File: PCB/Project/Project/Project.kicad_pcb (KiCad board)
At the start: 2 copper layers, 72.4 x 71.1 mm, 10 parts, among them J1 Conn_01x03_Male, J2 DB9_Female, SW1 SW_Push, U1 ESP32-DEVKIT-V1

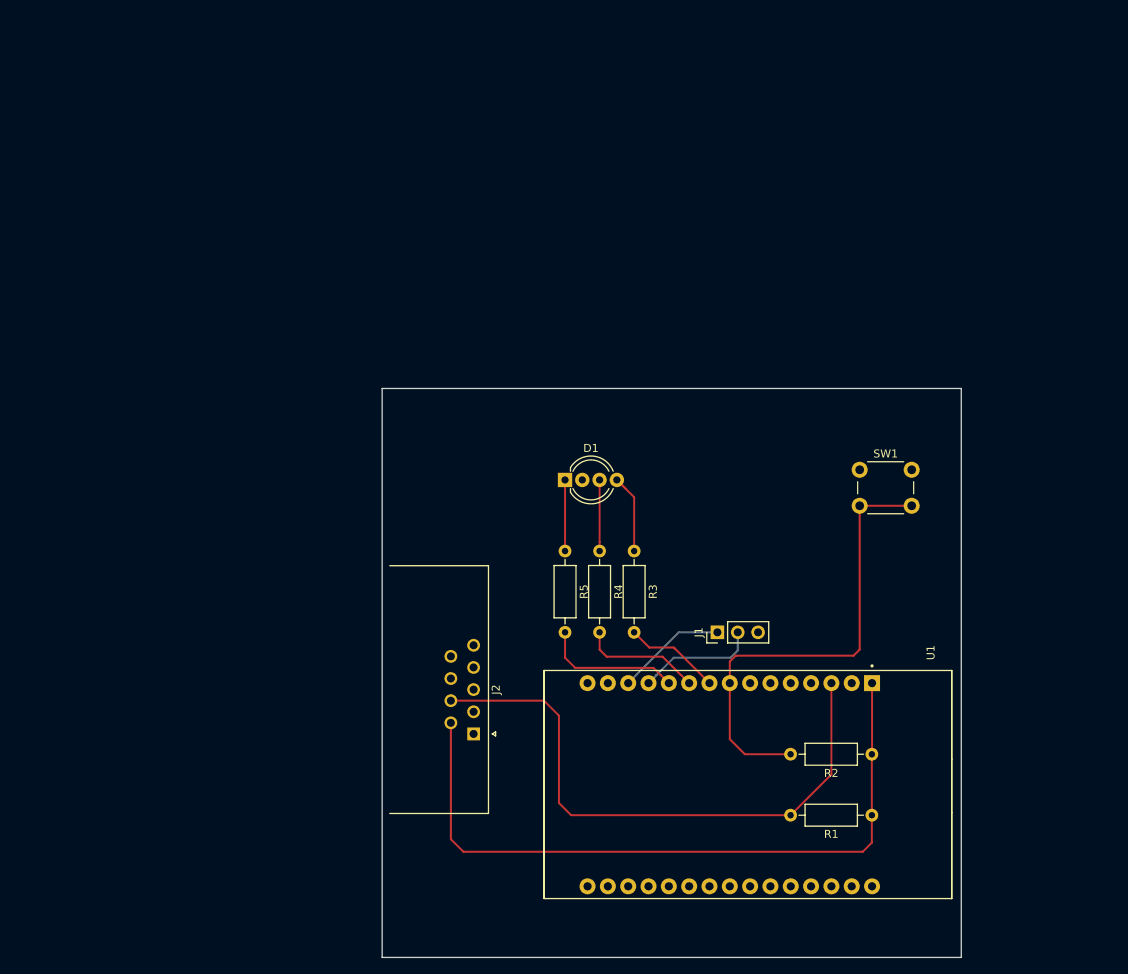
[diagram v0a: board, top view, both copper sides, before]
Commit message: New PCB. Added design rules.
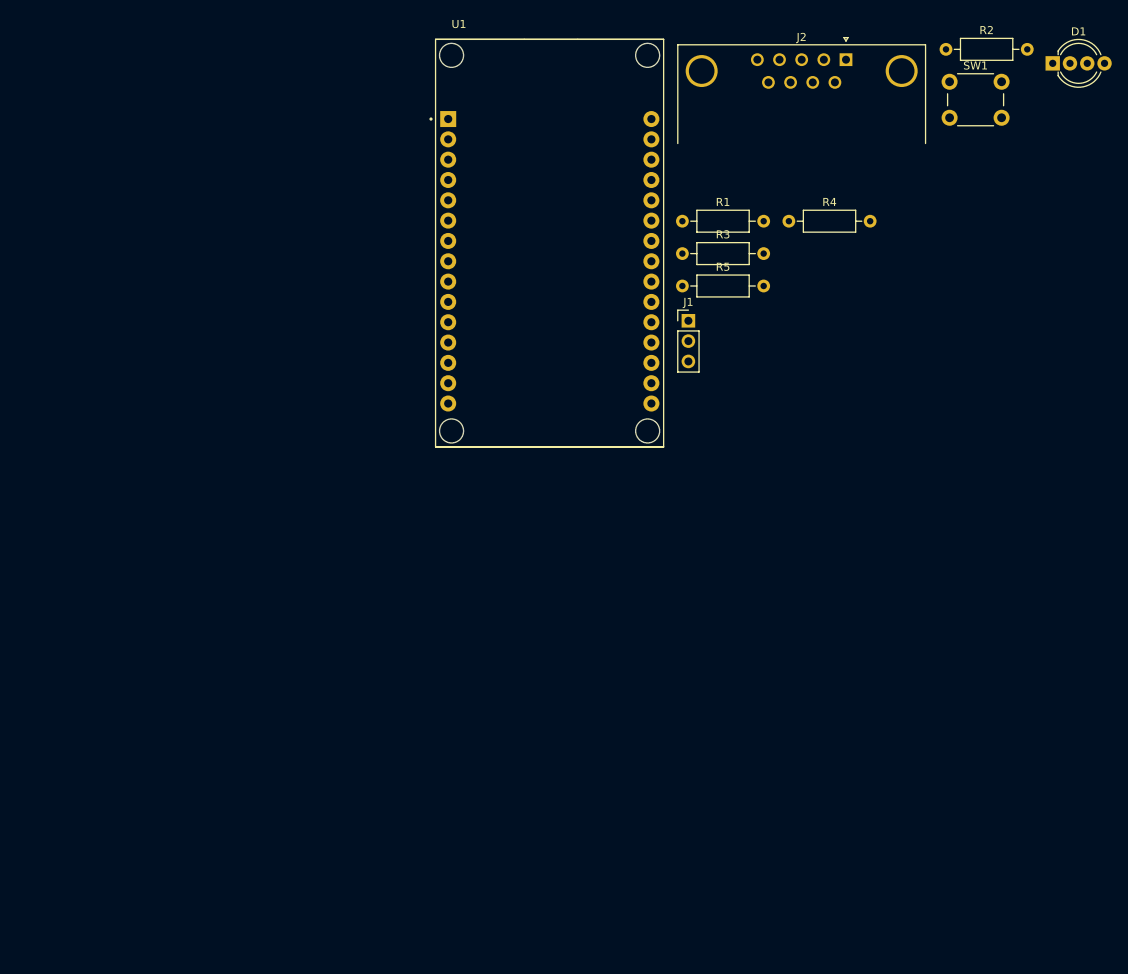
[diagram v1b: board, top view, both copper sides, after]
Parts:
- moved J2 96.3 mm to (138.0, 56.7), turned to 0 degrees
- moved R2 88.6 mm to (150.5, 55.4), turned to 0 degrees
- moved D1 80.2 mm to (163.8, 57.1)
- moved R1 77.9 mm to (117.5, 76.9), turned to 0 degrees
- moved U1 72.1 mm to (101.0, 79.6), turned to 0 degrees
- moved SW1 49.8 mm to (150.9, 59.5)
- moved R4 47.5 mm to (130.8, 76.9), turned to 0 degrees
- moved J1 39.1 mm to (118.3, 89.3), turned to 0 degrees
- moved R3 37.7 mm to (117.5, 80.9), turned to 0 degrees
- moved R5 36.2 mm to (117.5, 85.0), turned to 0 degrees
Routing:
- net +3V3: track 88.2 -> 0.00 mm
- net DATA: track 73.4 -> 0.00 mm
- net BTN: track 59.4 -> 0.00 mm
- net LED_RED: track 17.5 -> 0.00 mm
- net RXD: track 15.1 -> 0.00 mm
- net LED_GREEN: track 15.1 -> 0.00 mm
- net TXD: track 13.8 -> 0.00 mm
- net LED_BLUE: track 12.0 -> 0.00 mm
- net Net-(D1-Pad4): track 11.4 -> 0.00 mm
- net Net-(D1-Pad3): track 8.89 -> 0.00 mm
- net Net-(D1-Pad1): track 8.89 -> 0.00 mm
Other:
- board outline removed
- net class Power added: clearance 0.4, trace_width 0.5, via_dia 0.8, via_drill 0.4
- rule pad_to_mask_clearance: 0.051 -> 0.05
- rule solder_mask_min_width: 0.25 -> 0.3

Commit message: Finished routing
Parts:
- moved D1 86.9 mm to (85.1, 94.0)
- moved J2 78.0 mm to (101.6, 125.7)
- moved R2 77.4 mm to (100.3, 114.3), turned to 90 degrees
- moved U1 55.7 mm to (54.6, 110.5), turned to 180 degrees
- moved SW1 55.6 mm to (105.4, 91.4)
- moved R1 54.3 mm to (83.8, 119.4)
- moved R4 50.0 mm to (88.9, 104.1), turned to 270 degrees
- moved R5 37.7 mm to (85.1, 104.1), turned to 270 degrees
- moved R3 34.0 mm to (92.7, 104.1), turned to 270 degrees
- moved J1 18.5 mm to (111.8, 106.7)
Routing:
- net +3V3: track 0.00 -> 75.1 mm
- net BTN: track 0.00 -> 52.7 mm
- net TXD: track 0.00 -> 49.7 mm
- net RXD: track 0.00 -> 49.1 mm
- net DATA: track 0.00 -> 39.7 mm
- net LED_BLUE: track 0.00 -> 35.0 mm
- net LED_GREEN: track 0.00 -> 32.3 mm
- net LED_RED: track 0.00 -> 29.9 mm
- net Net-(D1-Pad4): track 0.00 -> 10.6 mm
- net Net-(D1-Pad3): track 0.00 -> 10.4 mm
- net Net-(D1-Pad1): track 0.00 -> 10.2 mm
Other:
- board outline added: 80 x 50.8 mm
- board text added: "Debug"
- board text added: "ESP32 Thermometer v0.1 Wojciech Zieliński 2022"
- board text added: "GN"
- board text added: "RX"
- board text added: "TX"

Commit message: PCB version 0.1
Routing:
- net GND: track 0.00 -> 10.2 mm, vias 0 -> 122
- net +3V3: track 75.1 -> 74.6 mm
- added copper zone on B.Cu, net GND
- added copper zone on F.Cu, net GND

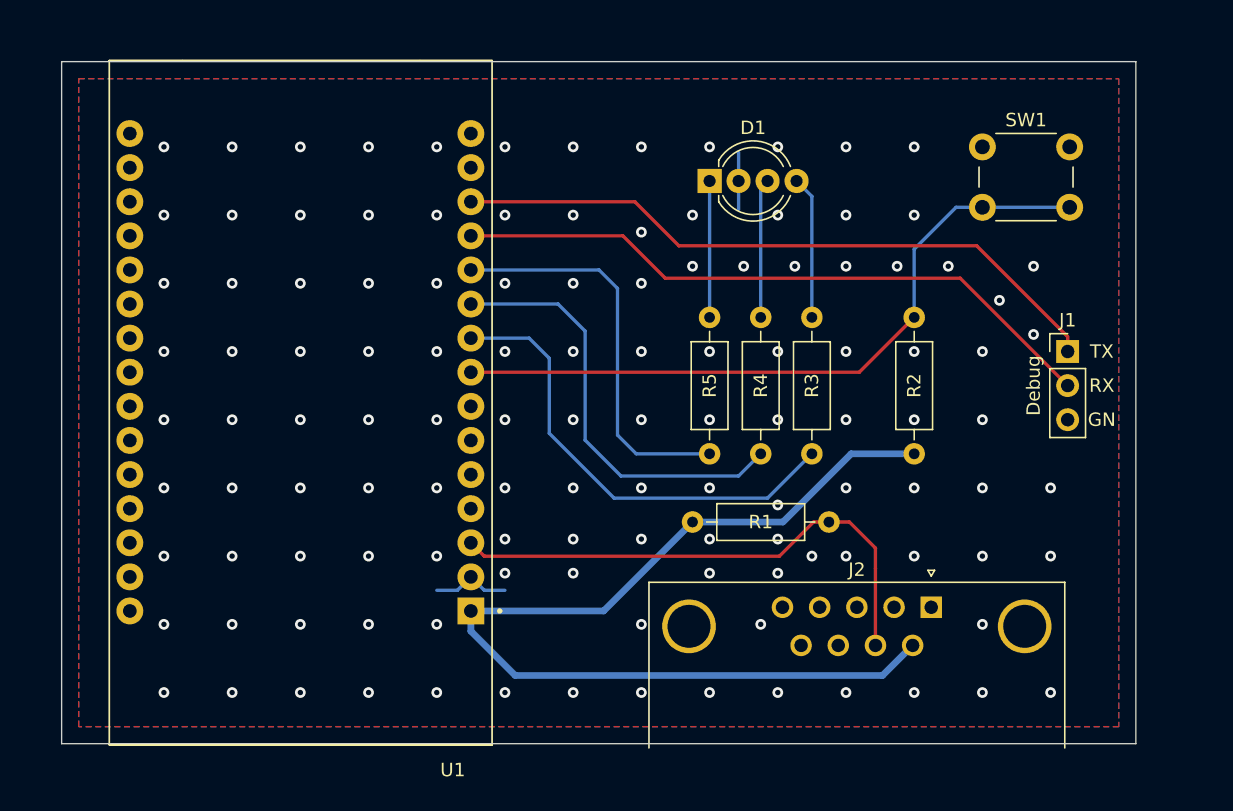
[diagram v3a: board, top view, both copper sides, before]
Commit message: Added mounting points on PCB. Generated gerbers.
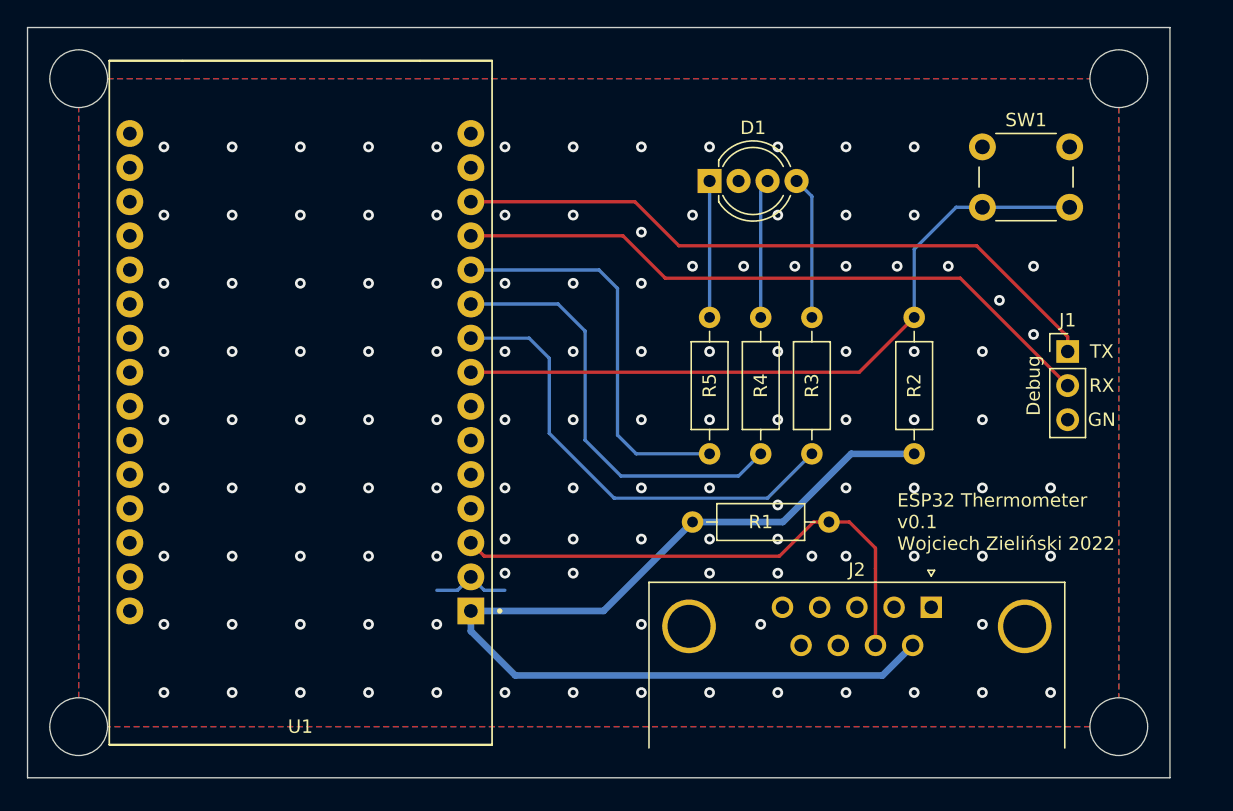
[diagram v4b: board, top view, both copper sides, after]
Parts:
- added REF**: MountingHole_4.3mm_M4, MountingHole:MountingHole_4.3mm_M4, F.Cu at (38.1, 86.4)
- added REF**: MountingHole_4.3mm_M4, MountingHole:MountingHole_4.3mm_M4, F.Cu at (115.6, 86.4)
- added REF**: MountingHole_4.3mm_M4, MountingHole:MountingHole_4.3mm_M4, F.Cu at (115.6, 134.6)
- added REF**: MountingHole_4.3mm_M4, MountingHole:MountingHole_4.3mm_M4, F.Cu at (38.1, 134.6)
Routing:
- net GND: track 10.2 -> 5.90 mm
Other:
- board size 80 x 50.8 mm -> 85.1 x 55.9 mm
- net class Default removed
- net class Power removed
